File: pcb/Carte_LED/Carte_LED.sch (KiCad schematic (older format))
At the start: 13 parts, among them J1 Conn_01x02

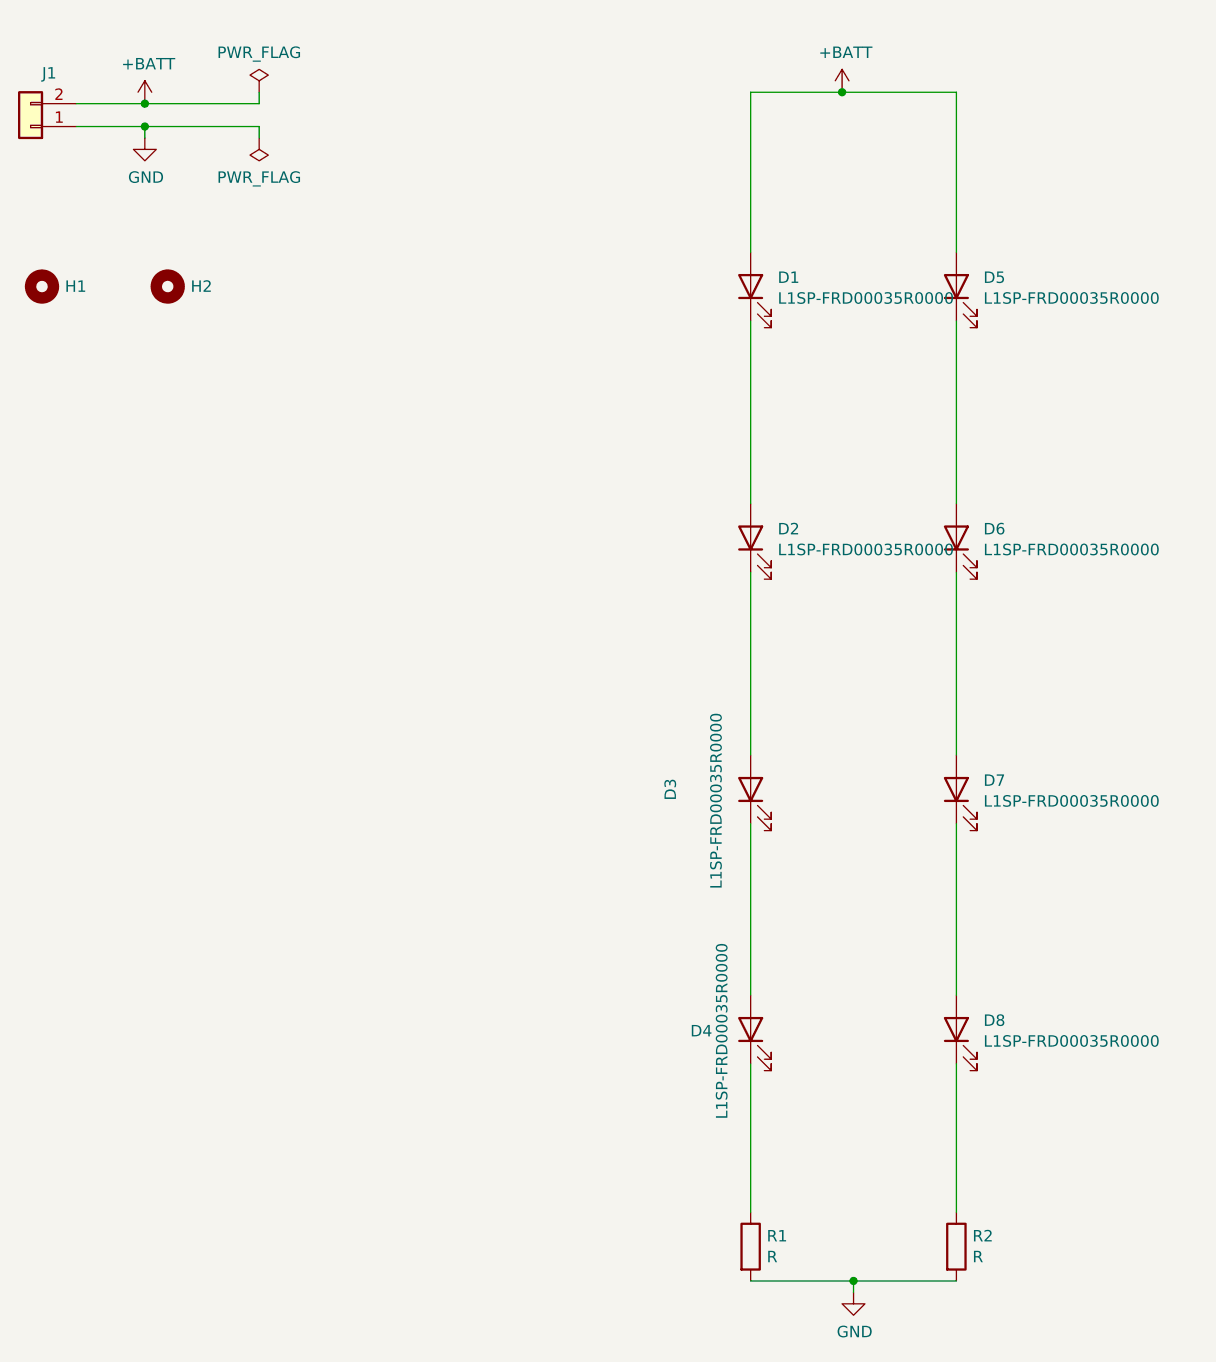
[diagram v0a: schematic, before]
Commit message: ajout de la carte chassi DFRobotics + creation d'une nouvelle carte led + creation d'une carte capteur pour DFRobotic + correction de l'alimentation en 5V des encodeurs sur DFRobotic (carte Landzo a corriger dans un prochaine commit)
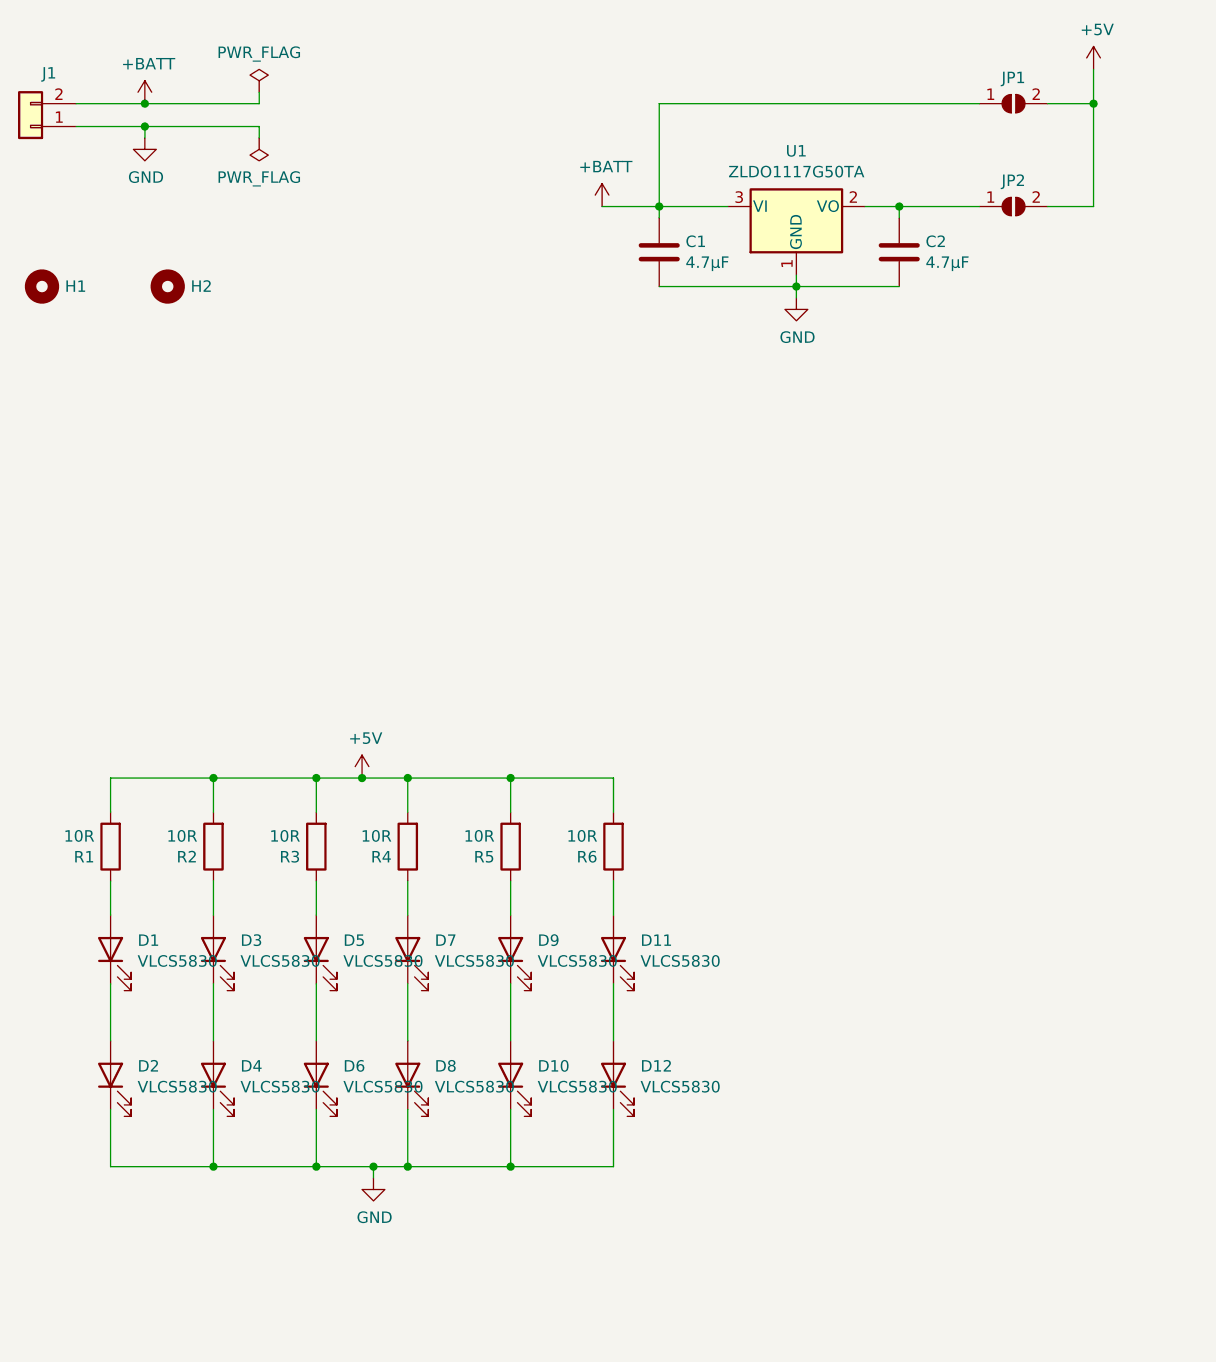
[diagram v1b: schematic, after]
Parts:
- added C1, C2: 4.7µF, Capacitor_SMD:C_1206_3216Metric_Pad1.42x1.75mm_HandSolder, symbol Device:C
- added D10, D11, D12, D9: VLCS5830, LED_THT:LED_D5.0mm_Clear, symbol Device:LED
- added JP1, JP2: SolderJumper_2_Open, Jumper:SolderJumper-2_P1.3mm_Open_RoundedPad1.0x1.5mm, symbol Jumper:SolderJumper_2_Open
- added R3, R4, R5, R6: 10R, Resistor_THT:R_Axial_DIN0309_L9.0mm_D3.2mm_P2.54mm_Vertical, symbol Device:R
- added U1: ZLDO1117G50TA, Package_TO_SOT_SMD:SOT-223-3_TabPin2, symbol Regulator_Linear:AMS1117-5.0
- D1, D2, D3, D4, D5, D6, D7, D8: value L1SP-FRD00035R0000 -> VLCS5830; footprint LED_SMD:LED_PLCC_2835_Handsoldering -> LED_THT:LED_D5.0mm_Clear
- R1, R2: value R -> 10R; footprint Resistor_THT:R_Axial_DIN0309_L9.0mm_D3.2mm_P12.70mm_Horizontal -> Resistor_THT:R_Axial_DIN0309_L9.0mm_D3.2mm_P2.54mm_Vertical
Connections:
- net +BATT: now also C1.1, JP1.1 (A), U1.3 (VI); no longer D1.2 (A), D5.2 (A)
- net GND: now also D2.1 (K), D4.1 (K), D6.1 (K), D8.1 (K), C1.2, C2.2, D10.1 (K), D12.1 (K), U1.1 (GND); no longer R1.2, R2.2
- net at D3.2 (A): now also R2.1; no longer D2.1 (K)
- net at R1.1: now also D1.2 (A); no longer D4.1 (K)
- net at D7.2 (A): now also R4.1; no longer D6.1 (K)
- new net: C2.1, JP2.1 (A), U1.2 (VO)
- new net: D5.2 (A), R3.1
- new net: D9.2 (A), R5.1
- new net: D10.2 (A), D9.1 (K)
- new net: D11.2 (A), R6.1
- new net: D11.1 (K), D12.2 (A)
- new net +5V: JP1.2 (B), JP2.2 (B), R1.2, R2.2, R3.2, R4.2, R5.2, R6.2
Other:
- moved on the sheet: R1
